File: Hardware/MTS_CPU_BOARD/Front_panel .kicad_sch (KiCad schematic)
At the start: 4 parts

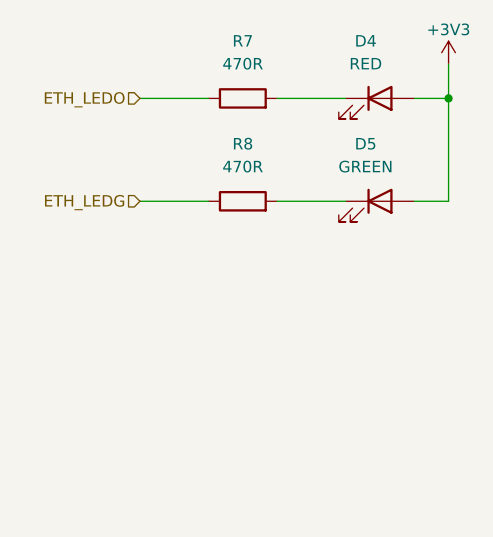
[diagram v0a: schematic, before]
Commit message: Add status Led´s
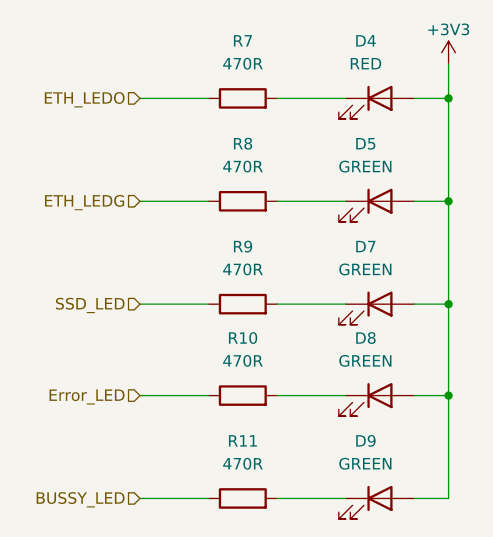
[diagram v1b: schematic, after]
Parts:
- added D7, D8, D9: GREEN, LED_THT:LED_D1.8mm_W3.3mm_H2.4mm, symbol Device:LED
- added R10, R11, R9: 470R, Resistor_SMD:R_0805_2012Metric, symbol Device:R
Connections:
- net +3V3: now also D7.2 (A), D8.2 (A), D9.2 (A)
- new net: D9.1 (K), R11.2
- new net: D7.1 (K), R9.2
- new net: D8.1 (K), R10.2
- new net BUSSY_LED: R11.1
- new net Error_LED: R10.1
- new net SSD_LED: R9.1
